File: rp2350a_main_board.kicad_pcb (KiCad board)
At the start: 2 copper layers, 61 x 45.7 mm, 65 parts, among them J1 USB_C_Receptacle_USB2.0_16P, J2 Micro_SD_Card_Det1, J3 Conn_02x10_Odd_Even, J4 SM03B-SRSS-TB, J5 SM03B-SRSS-TB, J6 Conn_02x10_Odd_Even, SW1 SW_Push, SW2 SW_Push, U1 RP2350_60QFN, U2 W25Q16JVSS, U3 APS1604M-3SQRx-SN, U4 AP2112K-3.3, Y1 ABM8-272-T3

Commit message: V1.0.0
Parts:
- removed C12: 100n, Capacitor_SMD:C_0402_1005Metric_Pad0.74x0.62mm_HandSolder
- removed C24: 10u, Capacitor_SMD:C_0603_1608Metric_Pad1.08x0.95mm_HandSolder
- removed RN1, RN2: 10k, Resistor_SMD:R_Array_Convex_4x0603
- added J7: Conn_02x12, Connector_PinSocket_2.54mm:PinSocket_2x12_P2.54mm_Vertical_SMD, F.Cu at (29.2, 45.7)
- added J8: Conn_02x12, Connector_PinSocket_2.54mm:PinSocket_2x12_P2.54mm_Vertical_SMD, F.Cu at (85.1, 45.7)
- added L2: 470n, Library:Inductor_SMD_L_4.0x4.0_H1.5, F.Cu at (75.6, 45.1)
- added R20: 511k, Resistor_SMD:R_0402_1005Metric_Pad0.72x0.64mm_HandSolder, F.Cu at (73.0, 39.4)
- added R21: 91k, Resistor_SMD:R_0402_1005Metric_Pad0.72x0.64mm_HandSolder, F.Cu at (75.1, 38.7)
- added R22: 10k, Resistor_SMD:R_0402_1005Metric_Pad0.72x0.64mm_HandSolder, F.Cu at (77.6, 38.7)
- added R23: 10k, Resistor_SMD:R_0402_1005Metric_Pad0.72x0.64mm_HandSolder, F.Cu at (80.0, 33.0)
- added R24: 10k, Resistor_SMD:R_0402_1005Metric_Pad0.72x0.64mm_HandSolder, F.Cu at (75.6, 33.0)
- added R25: 33k, Resistor_SMD:R_0402_1005Metric_Pad0.72x0.64mm_HandSolder, F.Cu at (75.6, 34.3)
- added SW3: SW_SPDT, Button_Switch_SMD:SW_SPDT_CK_JS102011SAQN, F.Cu at (76.8, 27.3)
- added TP1: ST, TestPoint:TestPoint_Pad_D1.0mm, F.Cu at (77.5, 36.8)
- added TP2: EN, TestPoint:TestPoint_Pad_D1.0mm, F.Cu at (72.4, 36.8)
- added TP4: PG, TestPoint:TestPoint_Pad_D1.0mm, F.Cu at (69.8, 39.6)
- added U5: TPS2116DRL, Package_TO_SOT_SMD:SOT-583-8, F.Cu at (78.1, 33.7)
- C3, C4: footprint Capacitor_SMD:C_0603_1608Metric_Pad1.08x0.95mm_HandSolder -> Capacitor_SMD:C_0402_1005Metric_Pad0.74x0.62mm_HandSolder
- D1, D2: footprint LED_SMD:LED_0805_2012Metric -> LED_SMD:LED_0805_2012Metric_Pad1.15x1.40mm_HandSolder
- J3, J6: value Conn_02x10_Odd_Even -> Conn_02x12; footprint Connector_PinSocket_2.54mm:PinSocket_2x10_P2.54mm_Vertical -> Connector_PinSocket_2.54mm:PinSocket_2x12_P2.54mm_Vertical
- R1, R2, R6, R7, R8, R9: footprint Resistor_SMD:R_0805_2012Metric_Pad1.20x1.40mm_HandSolder -> Resistor_SMD:R_0402_1005Metric_Pad0.72x0.64mm_HandSolder
- R11: value 470 -> 1k; footprint Resistor_SMD:R_0603_1608Metric_Pad0.98x0.95mm_HandSolder -> Resistor_SMD:R_0402_1005Metric_Pad0.72x0.64mm_HandSolder
- U4: value AP2112K-3.3 -> TPS63802; footprint Package_TO_SOT_SMD:SOT-23-5 -> Library:TPS63802
- moved J6 58.0 mm to (86.4, 31.8)
- moved J3 55.5 mm to (30.5, 31.8)
- moved SW2 28.6 mm to (35.6, 64.1)
- moved R12 28.5 mm to (50.0, 54.9), turned to 180 degrees
- moved R11 21.6 mm to (54.0, 27.9), turned to 0 degrees
- moved R7 21.4 mm to (39.0, 64.1)
- moved SW1 14.4 mm to (42.4, 64.1), turned to 180 degrees
- moved D1 13.6 mm to (58.4, 26.7), turned to 180 degrees
- moved C22 9.09 mm to (71.1, 42.5)
- moved C21 8.24 mm to (78.0, 41.1), turned to 90 degrees
- moved R6 7.94 mm to (45.8, 64.1)
- moved U4 7.24 mm to (75.6, 41.3)
- moved C23 7.10 mm to (72.6, 42.5), turned to -90 degrees
- moved J4 5.46 mm to (79.1, 62.9)
- moved J5 5.36 mm to (71.8, 62.9)
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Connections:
- C21 pad 1: VBUS -> VIN
- C22 pad 1: VBUS -> +3V3
- J1 pad A4: VBUS -> VUSB
- J1 pad A9: VBUS -> VUSB
- J1 pad B4: VBUS -> VUSB
- J1 pad B9: VBUS -> VUSB
- J3 pad 1: VBUS -> +3V3
- J3 pad 10: GND -> /GPIO10
- J3 pad 11: /GPIO25 -> GND
- J3 pad 12: /GPIO24 -> GND
- J3 pad 13: /GPIO23 -> /GPIO13
- J3 pad 14: /GPIO22 -> /GPIO12
- J3 pad 15: GND -> /GPIO15
- J3 pad 16: GND -> /GPIO14
- J3 pad 17: /GPIO21 -> GND
- J3 pad 18: /GPIO20 -> GND
- J3 pad 19: GND -> /GPIO17
- J3 pad 2: VBUS -> +3V3
- J3 pad 20: GND -> /GPIO16
- J3 pad 5: /GPIO29_ADC3 -> GND
- J3 pad 6: /GPIO28_ADC2 -> GND
- J3 pad 7: /GPIO27_ADC1 -> /GPIO9
- J3 pad 8: /GPIO26_ADC0 -> /RUN
- J3 pad 9: GND -> /GPIO11
- J6 pad 1: +3V3 -> VUSB
- J6 pad 10: /GPIO13 -> /GPIO29_ADC3
- J6 pad 11: /GPIO14 -> /GPIO26_ADC0
- J6 pad 12: /GPIO15 -> /GPIO27_ADC1
- J6 pad 15: /GPIO16 -> /GPIO24
- J6 pad 16: /GPIO17 -> /GPIO25
- J6 pad 17: /GPIO18 -> /GPIO22
- J6 pad 18: /GPIO19 -> /GPIO23
- J6 pad 2: +3V3 -> VUSB
- J6 pad 3: GND -> VBAT
- J6 pad 4: GND -> VBAT
- J6 pad 5: /RUN -> VIN
- J6 pad 6: /GPIO11 -> VIN
- J6 pad 7: GND -> +3V3
- J6 pad 8: GND -> +3V3
- J6 pad 9: /GPIO12 -> /GPIO28_ADC2
- U1 pad 15: GND -> /GPIO11
- U1 pad 17: GND -> /GPIO13
- U1 pad 19: GND -> /GPIO15
- U1 pad 28: GND -> /GPIO17
- U1 pad 31: GND -> /GPIO19
- U4 pad 1: VBUS -> Net-(U4-EN)
- U4 pad 3: VBUS -> GND
- U4 pad 4: unconnected-(U4-NC-Pad4) -> Net-(U4-FB)
- U4 pad 5: +3V3 -> Net-(U4-PG)
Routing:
- net VBUS: track 40.1 -> 0.00 mm
- net VUSB: track 0.00 -> 38.9 mm, vias 0 -> 3
- net Net-(D2-A): track 1.87 -> 35.7 mm, vias 0 -> 2
- net /GPIO9: track 8.05 -> 37.0 mm
- net VIN: track 0.00 -> 26.1 mm, vias 0 -> 1
- net +3V3: track 205.5 -> 186.9 mm, vias 16 -> 13
- net /SD_CLK: track 23.2 -> 10.5 mm, vias 2 -> 0
- net /SD_CMD: track 25.9 -> 14.0 mm, vias 2 -> 0
- net /GPIO28_ADC2: track 15.2 -> 26.8 mm
- net /GPIO26_ADC0: track 14.6 -> 25.0 mm
- net /GPIO12: track 36.1 -> 46.0 mm
- net /SD_D0: track 22.5 -> 13.0 mm
- net /GPIO14: track 36.6 -> 46.1 mm
- net /GPIO15: track 39.9 -> 48.7 mm
- net /SD_D3/CD: track 28.3 -> 19.9 mm
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- added copper zone on B.Cu, net +3V3
- added copper zone on F.Cu, net /PS_L1
- added copper zone on F.Cu, net /PS_L2
- added copper zone on F.Cu, net VIN
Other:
- board size 61 x 45.7 mm -> 63.5 x 40.6 mm
- board text added: "Main Board"
- board text added: "OFF ON"
- board text added: "ON OFF"
- board text added: "PG"
- board text added: "RP2350A Main Board"
- board text added: "USB"
- board text added: "V1.0.0"
- board text added: "microSD"
- board text added: "~{EN}"
- board text added: "~{ST}"
- board text removed: "3V3 GND 11 RUN GND 13 12 15 14 GND 17 16 19 18 GND"
- board text removed: "ADC"
- board text removed: "HSTX"
- board text removed: "Test Board"
- board text removed: "V1.2.0"
- board text removed: "VIN 3V3 28 29 26 27 GND 24 25 22 23 GND 20 21 GND"

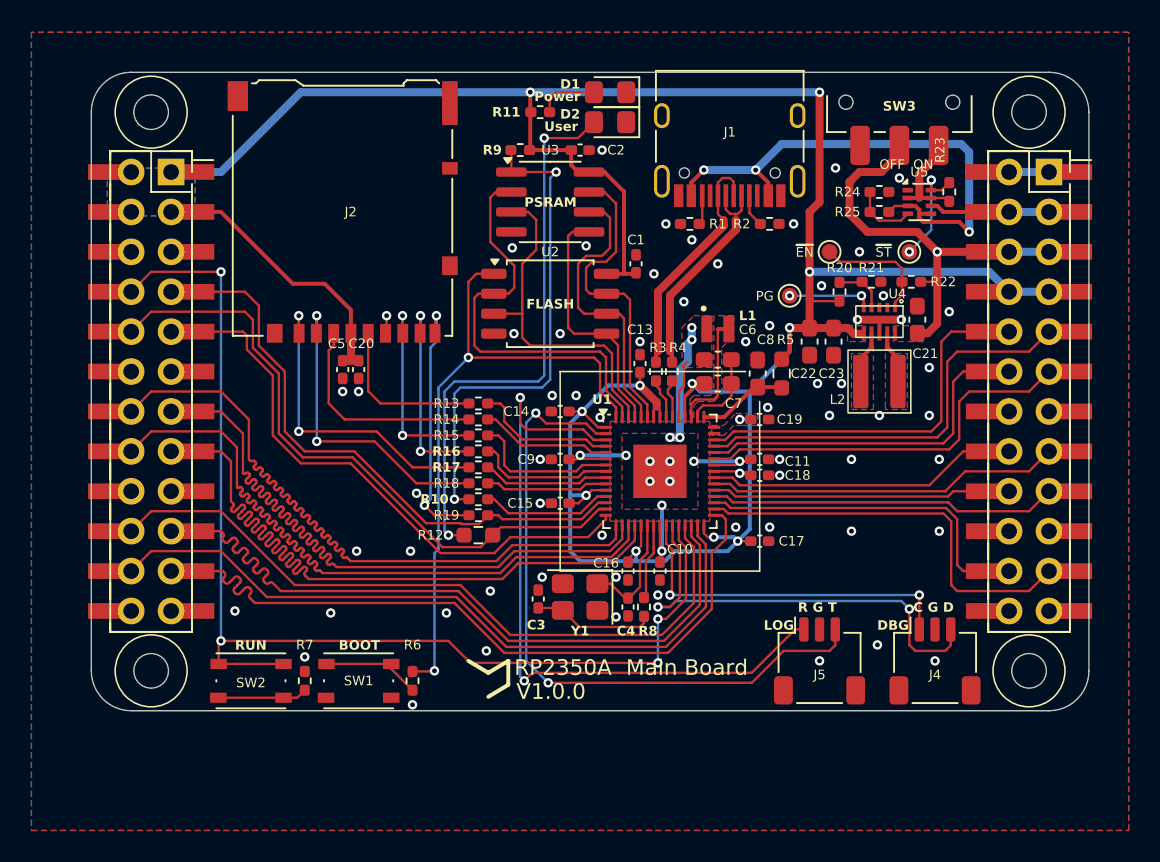
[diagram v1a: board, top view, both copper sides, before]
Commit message: Clean up component references
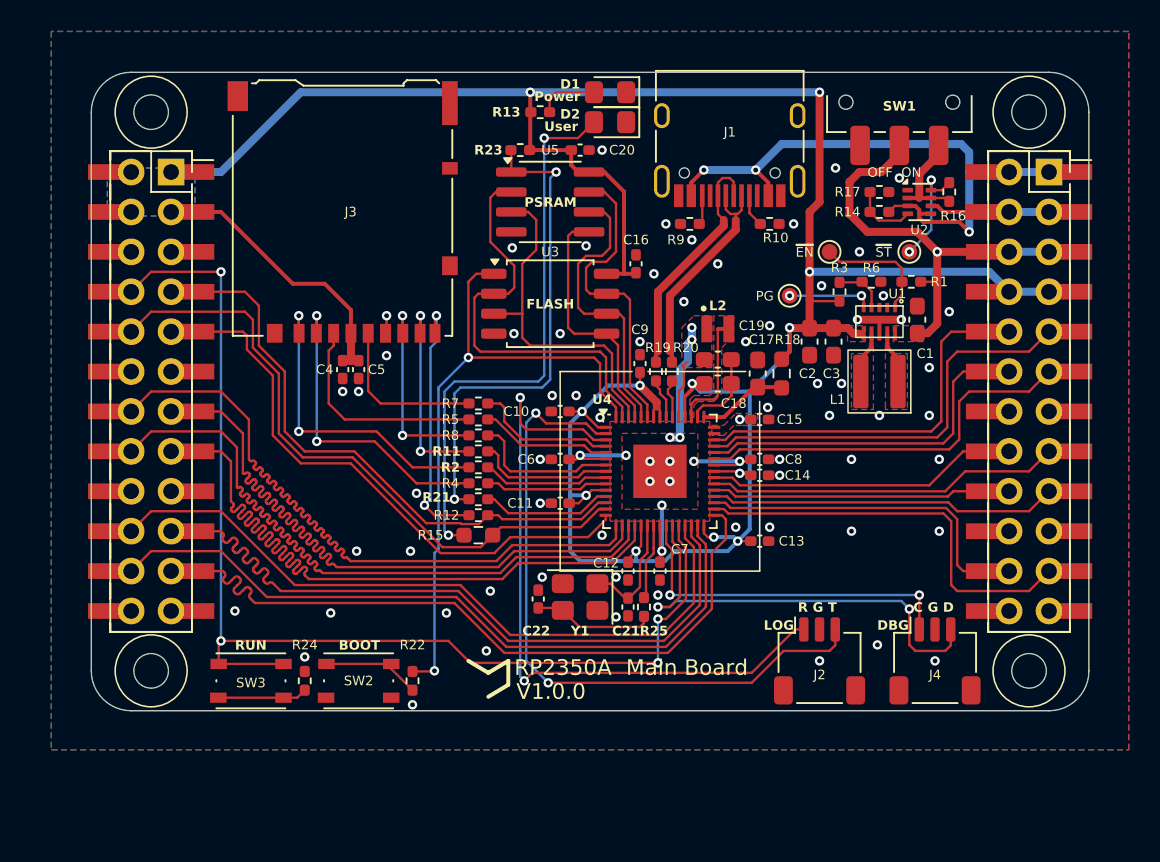
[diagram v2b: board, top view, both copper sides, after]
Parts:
- renumbered C21 to C1, C14 to C10, C15 to C11, C16 to C12, C17 to C13, C18 to C14, C19 to C15, C1 to C16, C8 to C17, C7 to C18, C6 to C19, C22 to C2, C2 to C20, C4 to C21, C3 to C22, C23 to C3, C5 to C4, C20 to C5, C9 to C6, C10 to C7, C11 to C8, C13 to C9, J5 to J2, J2 to J3, J3 to J5, L2 to L1, L1 to L2, R22 to R1, R2 to R10, R16 to R11, R19 to R12, R11 to R13, R25 to R14, R12 to R15, R23 to R16, R24 to R17, R5 to R18, R3 to R19, R17 to R2, R4 to R20, R10 to R21, R6 to R22, R9 to R23, R7 to R24, R8 to R25, R20 to R3, R18 to R4, R14 to R5, R21 to R6, R13 to R7, R15 to R8, R1 to R9, SW3 to SW1, SW1 to SW2, SW2 to SW3, TP2 to TP1, TP4 to TP2, TP1 to TP3, U4 to U1, U5 to U2, U2 to U3, U1 to U4, U3 to U5
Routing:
- net GND: vias 67 -> 68

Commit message: Update BOM list
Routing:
- net Net-(SW1-A): track 6.59 -> 5.06 mm
- added copper zone on F.Cu, net Net-(SW1-A)
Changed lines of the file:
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@@
 		(sheetname "/")
 		(sheetfile "rp2350a_main_board.kicad_sch")
-		(attr smd exclude_from_bom)
+		(attr smd)
 		(fp_line
 			(start -0.167621 0.38)
@@
 		(sheetname "/")
 		(sheetfile "rp2350a_main_board.kicad_sch")
-		(attr smd exclude_from_bom)
+		(attr smd)
 		(fp_line
 			(start -0.167621 0.38)
@@
 		(sheetname "/")
 		(sheetfile "rp2350a_main_board.kicad_sch")
-		(attr smd exclude_from_bom)
+		(attr smd)
 		(fp_line
 			(start -0.167621 -0.38)
@@
 	)
 	(via
-		(at 75.565 47.244)
+		(at 75.565 47.371)
 		(size 0.6)
 		(drill 0.3)
@@
 	)
 	(segment
-		(start 78.105 33.405)
-		(end 78.105 31.877)
-		(width 0.508)
-		(layer "F.Cu")
-		(net 73)
-	)
-	(segment
 		(start 78.105 31.877)
 		(end 79.335 30.647)
@@
 	)
 	(zone
+		(net 73)
+		(net_name "Net-(SW1-A)")
+		(layer "F.Cu")
+		(hatch edge 0.5)
+		(priority 9)
+		(connect_pads
+			(clearance 0.1524)
+		)
+		(min_thickness 0.1524)
+		(filled_areas_thickness no)
+		(fill yes
+			(thermal_gap 0.1524)
+			(thermal_bridge_width 0.254)
+		)
+		(polygon
+			(pts
+				(xy 77.851 31.877) (xy 78.359 31.877) (xy 78.359 33.528) (xy 77.851 33.528) (xy 77.851 31.877)
+			)
+		)
+	)
+	(zone

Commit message: Add text, Add part name to L1
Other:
- board text added: "10 - BUILT-IN LED"
- board text added: "11 10"
- board text added: "12 13"
- board text added: "13 12"
- board text added: "14 15"
- board text added: "15 14"
- board text added: "16 17"
- board text added: "17 16"
- board text added: "18 19"
- board text added: "19 18"
- board text added: "20 21"
- board text added: "21 20"
- board text added: "22 23"
- board text added: "23 22"
- board text added: "24 25"
- board text added: "25 24"
- board text added: "26 27"
- board text added: "27 26"
- board text added: "28 29"
- board text added: "29 28"
- board text added: "3V3"
- board text added: "9 - SD DETECT"
- board text added: "9 RUN"
- board text added: "ADC"
- board text added: "GND"
- board text added: "HSTX"
- board text added: "VBAT"
- board text added: "VIN"
- board text added: "VUSB"
